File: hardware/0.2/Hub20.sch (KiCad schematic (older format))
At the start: 130 parts, among them J1 USB_C_Receptacle_USB2.0, Q1 DTC123J, Q2 BSS138, SW1 SW_Push, SW10 MX_RGB, SW11 MX_RGB, SW12 MX_RGB, SW13 Rotary_Encoder_Switch, SW14 MX_RGB, SW15 MX_RGB, SW16 MX_RGB, SW17 MX_RGB, SW18 MX_RGB, SW19 MX_RGB, SW2 MX_RGB, SW20 MX_RGB, SW21 MX_RGB, SW22 MX_RGB, SW23 MX_RGB, SW3 MX_RGB, SW4 MX_RGB, SW5 MX_RGB, SW6 MX_RGB, SW7 Rotary_Encoder_Switch, SW8 MX_RGB, SW9 MX_RGB, U1 AP2112K-3.3, U2 USBLC6-2SC6, U3 STM32F072C8Tx

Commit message: layout getting close
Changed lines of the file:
@@
 Wire Wire Line
 	2650 4500 2650 4550
-$Comp
-L power:+3V3 #PWR044
-U 1 1 5EF80615
-P 2750 3950
-F 0 "#PWR044" H 2750 3800 50  0001 C CNN
-F 1 "+3V3" H 2765 4123 50  0000 C CNN
-F 2 "" H 2750 3950 50  0001 C CNN
-F 3 "" H 2750 3950 50  0001 C CNN
-	1    2750 3950
-	1    0    0    -1
-$EndComp
 Wire Wire Line
 	2550 4100 2650 4100
@@
 U 1 1 5F48ECC9
 P 2550 2300
-F 0 "U2" H 2550 2981 50  0000 C CNN
-F 1 "USBLC6-2SC6" H 2550 2890 50  0000 C CNN
+F 0 "U2" H 2375 2600 50  0000 C CNN
+F 1 "USBLC6-2SC6" H 2850 2600 50  0000 C CNN
 F 2 "Package_TO_SOT_SMD:SOT-23-6" H 1800 2700 50  0001 C CNN
 F 3 "http://www2.st.com/resource/en/datasheet/CD00050750.pdf" H 2750 2650 50  0001 C CNN
@@
 $EndComp
 $Comp
-L power:+3V3 #PWR0101
-U 1 1 60B0E43F
-P 1000 6150
-F 0 "#PWR0101" H 1000 6000 50  0001 C CNN
-F 1 "+3V3" H 1015 6323 50  0000 C CNN
-F 2 "" H 1000 6150 50  0001 C CNN
-F 3 "" H 1000 6150 50  0001 C CNN
-	1    1000 6150
-	1    0    0    -1
-$EndComp
-$Comp
-L power:+3V3 #PWR0188
-U 1 1 60B0F88E
-P 8300 2650
-F 0 "#PWR0188" H 8300 2500 50  0001 C CNN
-F 1 "+3V3" H 8315 2823 50  0000 C CNN
-F 2 "" H 8300 2650 50  0001 C CNN
-F 3 "" H 8300 2650 50  0001 C CNN
-	1    8300 2650
-	1    0    0    -1
-$EndComp
-$Comp
-L power:+3V3 #PWR0189
-U 1 1 60B200DB
-P 9800 9800
-F 0 "#PWR0189" H 9800 9650 50  0001 C CNN
-F 1 "+3V3" H 9815 9973 50  0000 C CNN
-F 2 "" H 9800 9800 50  0001 C CNN
-F 3 "" H 9800 9800 50  0001 C CNN
-	1    9800 9800
-	1    0    0    -1
-$EndComp
-$Comp
 L Device:D_Small D26
 U 1 1 5F566ED0
@@
 LED_5V
 NoConn ~ 15850 7300
+$Comp
+L power:+3.3V #PWR0101
+U 1 1 5F3592B8
+P 2750 3950
+F 0 "#PWR0101" H 2750 3800 50  0001 C CNN
+F 1 "+3.3V" H 2765 4123 50  0000 C CNN
+F 2 "" H 2750 3950 50  0001 C CNN
+F 3 "" H 2750 3950 50  0001 C CNN
+	1    2750 3950
+	1    0    0    -1
+$EndComp
+$Comp
+L power:+3.3V #PWR0148
+U 1 1 5F3A0227
+P 1000 6150
+F 0 "#PWR0148" H 1000 6000 50  0001 C CNN
+F 1 "+3.3V" H 1015 6323 50  0000 C CNN
+F 2 "" H 1000 6150 50  0001 C CNN
+F 3 "" H 1000 6150 50  0001 C CNN
+	1    1000 6150
+	1    0    0    -1
+$EndComp
+$Comp
+L power:+3.3V #PWR0149
+U 1 1 5F4789D3
+P 9800 9800
+F 0 "#PWR0149" H 9800 9650 50  0001 C CNN
+F 1 "+3.3V" H 9815 9973 50  0000 C CNN
+F 2 "" H 9800 9800 50  0001 C CNN
+F 3 "" H 9800 9800 50  0001 C CNN
+	1    9800 9800
+	1    0    0    -1
+$EndComp
+$Comp
+L power:+3.3V #PWR0150
+U 1 1 5F4CF7BC
+P 8300 2650
+F 0 "#PWR0150" H 8300 2500 50  0001 C CNN
+F 1 "+3.3V" H 8300 2825 50  0000 C CNN
+F 2 "" H 8300 2650 50  0001 C CNN
+F 3 "" H 8300 2650 50  0001 C CNN
+	1    8300 2650
+	1    0    0    -1
+$EndComp
 $EndSCHEMATC

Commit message: tidy up things
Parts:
- SW1: value SW_Push -> KMR2
- SW13, SW7: value Rotary_Encoder_Switch -> EC11
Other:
- moved on the sheet: C10, C18, C19, C20, C28, C32, C34, C36, C38, C40, C48, C49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

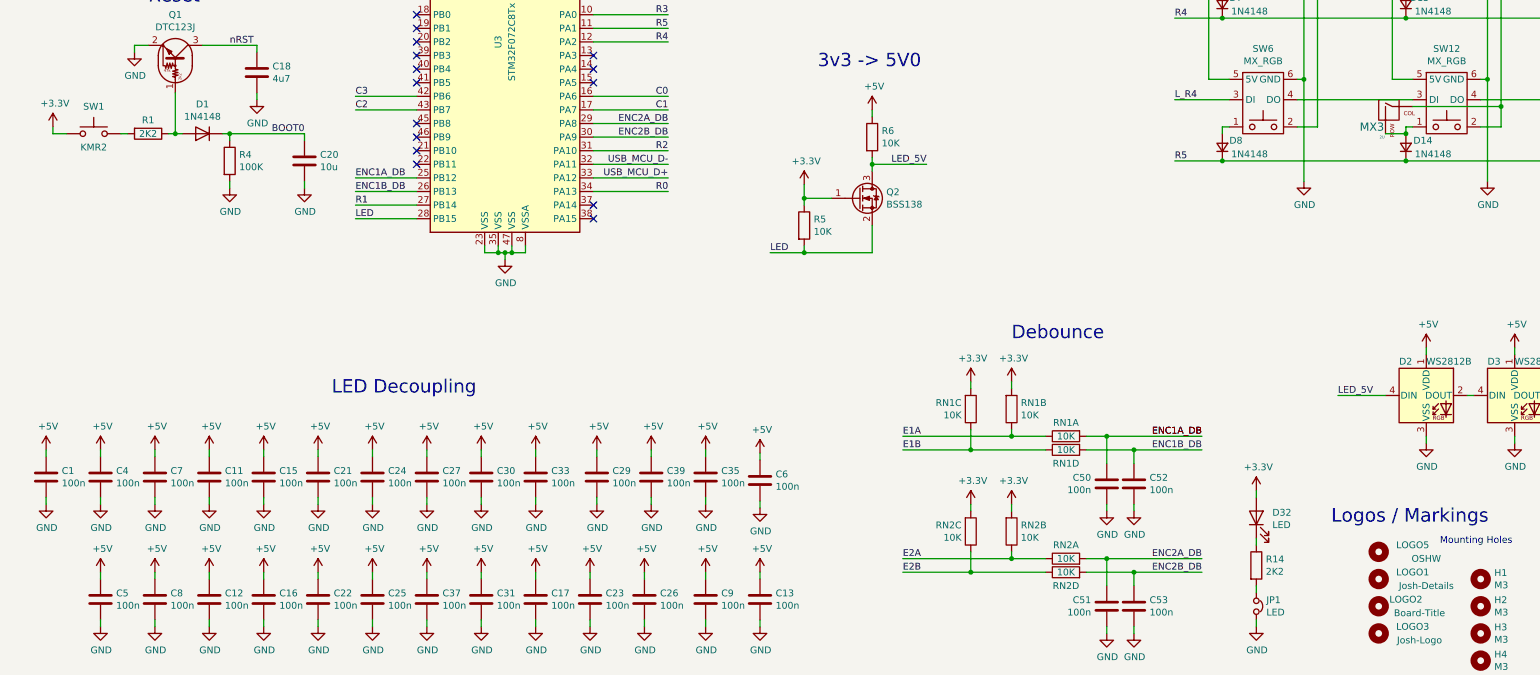
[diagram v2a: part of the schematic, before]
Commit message: side mounted rst + slik cleanup
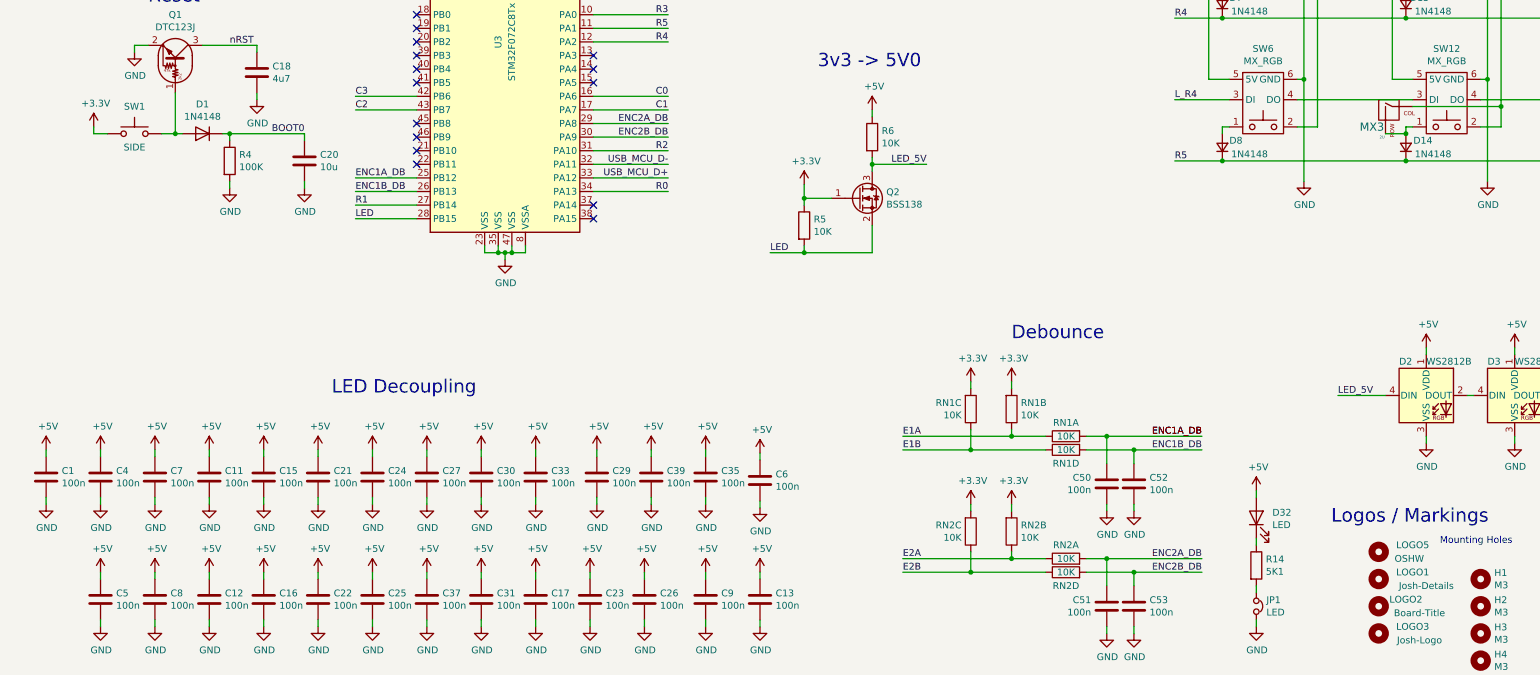
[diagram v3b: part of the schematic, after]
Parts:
- removed R1: 2K2, Resistor_SMD:R_0603_1608Metric, symbol Device:R
- LOGO3: footprint josh-logos:josh-johnson-logo-8_6x1_5 -> josh-logos:josh-johnson-logo-11x2
- LOGO5: footprint josh-logos:OSHW_Logo_3.6x3.6_F.Mask -> josh-logos:OSHW-Logo2_9.8x8mm_Mask
- R14: value 2K2 -> 5K1
- SW1: value KMR2 -> SIDE; footprint josh-buttons-switches:SW_Push_KMR2 -> josh-buttons-switches:Panasonic_EVQPUL_EVQPUC
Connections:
- net +3V3: no longer D32.2 (A)
- net +5V: now also D32.2 (A)
- net at D1.2 (A), Q1.1 (B): now also SW1.2
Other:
- moved on the sheet: SW1
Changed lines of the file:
@@
 F 0 "LOGO3" H 10950 10900 50  0000 C CNN
 F 1 "Josh-Logo" H 11000 10800 50  0000 C CNN
-F 2 "josh-logos:josh-johnson-logo-8_6x1_5" H 10700 10850 50  0001 C CNN
+F 2 "josh-logos:josh-johnson-logo-11x2" H 10700 10850 50  0001 C CNN
 F 3 "~" H 10700 10850 50  0001 C CNN
 	1    10700 10850
@@
 $EndComp
 $Comp
-L Mechanical:MountingHole LOGO2
-U 1 1 5E205A57
-P 10700 10650
-F 0 "LOGO2" H 10900 10700 50  0000 C CNN
-F 1 "Board-Title" H 11000 10600 50  0000 C CNN
-F 2 "josh-logos:board-title" H 10700 10650 50  0001 C CNN
-F 3 "~" H 10700 10650 50  0001 C CNN
-	1    10700 10650
-	1    0    0    -1
-$EndComp
-$Comp
 L Mechanical:MountingHole H3
 U 1 1 5EF4D892
@@
 $EndComp
 $Comp
-L Device:R R1
-U 1 1 5F123A6F
-P 1650 7175
-F 0 "R1" V 1550 7175 50  0000 C CNN
-F 1 "2K2" V 1650 7175 50  0000 C CNN
-F 2 "Resistor_SMD:R_0603_1608Metric" V 1580 7175 50  0001 C CNN
-F 3 "~" H 1650 7175 50  0001 C CNN
-	1    1650 7175
-	0    1    1    0
-$EndComp
-$Comp
 L Switch:SW_Push SW1
 U 1 1 5F124780
-P 1250 7175
-F 0 "SW1" H 1250 7375 50  0000 C CNN
-F 1 "KMR2" H 1250 7075 50  0000 C CNN
-F 2 "josh-buttons-switches:SW_Push_KMR2" H 1250 7375 50  0001 C CNN
-F 3 "~" H 1250 7375 50  0001 C CNN
-	1    1250 7175
+P 1550 7175
+F 0 "SW1" H 1550 7375 50  0000 C CNN
+F 1 "SIDE" H 1550 7075 50  0000 C CNN
+F 2 "josh-buttons-switches:Panasonic_EVQPUL_EVQPUC" H 1550 7375 50  0001 C CNN
+F 3 "~" H 1550 7375 50  0001 C CNN
+	1    1550 7175
 	1    0    0    -1
 $EndComp
@@
 $EndComp
 Wire Wire Line
-	950  7125 950  7175
+	1250 7125 1250 7175
 Wire Wire Line
-	950  7175 1050 7175
-Wire Wire Line
-	1450 7175 1500 7175
-Wire Wire Line
-	1800 7175 1850 7175
+	1250 7175 1350 7175
 Wire Wire Line
 	1850 6875 1850 7175
@@
 P 9800 10350
 F 0 "R14" H 9870 10396 50  0000 L CNN
-F 1 "2K2" H 9870 10305 50  0000 L CNN
+F 1 "5K1" H 9870 10305 50  0000 L CNN
 F 2 "Resistor_SMD:R_0603_1608Metric" V 9730 10350 50  0001 C CNN
 F 3 "~" H 9800 10350 50  0001 C CNN
@@
 P 10700 10250
 F 0 "LOGO5" H 10950 10300 50  0000 C CNN
-F 1 "OSHW" H 11050 10200 50  0000 C CNN
-F 2 "josh-logos:OSHW_Logo_3.6x3.6_F.Mask" H 10700 10250 50  0001 C CNN
+F 1 "OSHW" H 10925 10200 50  0000 C CNN
+F 2 "josh-logos:OSHW-Logo2_9.8x8mm_Mask" H 10700 10250 50  0001 C CNN
 F 3 "~" H 10700 10250 50  0001 C CNN
 	1    10700 10250
@@
 L power:+3.3V #PWR0148
 U 1 1 5F3A0227
-P 950 7125
-F 0 "#PWR0148" H 950 6975 50  0001 C CNN
-F 1 "+3.3V" H 965 7298 50  0000 C CNN
-F 2 "" H 950 7125 50  0001 C CNN
-F 3 "" H 950 7125 50  0001 C CNN
-	1    950  7125
-	1    0    0    -1
-$EndComp
-$Comp
-L power:+3.3V #PWR0149
-U 1 1 5F4789D3
-P 9800 9800
-F 0 "#PWR0149" H 9800 9650 50  0001 C CNN
-F 1 "+3.3V" H 9815 9973 50  0000 C CNN
-F 2 "" H 9800 9800 50  0001 C CNN
-F 3 "" H 9800 9800 50  0001 C CNN
-	1    9800 9800
+P 1250 7125
+F 0 "#PWR0148" H 1250 6975 50  0001 C CNN
+F 1 "+3.3V" H 1265 7298 50  0000 C CNN
+F 2 "" H 1250 7125 50  0001 C CNN
+F 3 "" H 1250 7125 50  0001 C CNN
+	1    1250 7125
 	1    0    0    -1
 $EndComp
@@
 3v3 -> 5V0
 Connection ~ 5275 4600
+$Comp
+L Mechanical:MountingHole LOGO2
+U 1 1 5E205A57
+P 10700 10650
+F 0 "LOGO2" H 10900 10700 50  0000 C CNN
+F 1 "Board-Title" H 11000 10600 50  0000 C CNN
+F 2 "josh-logos:board-title" H 10700 10650 50  0001 C CNN
+F 3 "~" H 10700 10650 50  0001 C CNN
+	1    10700 10650
+	1    0    0    -1
+$EndComp
+$Comp
+L power:+5V #PWR0149
+U 1 1 5F4C0452
+P 9800 9800
+F 0 "#PWR0149" H 9800 9650 50  0001 C CNN
+F 1 "+5V" H 9815 9973 50  0000 C CNN
+F 2 "" H 9800 9800 50  0001 C CNN
+F 3 "" H 9800 9800 50  0001 C CNN
+	1    9800 9800
+	1    0    0    -1
+$EndComp
+Wire Wire Line
+	1750 7175 1850 7175
 $EndSCHEMATC

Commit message: update BOM
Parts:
- added D31, D33, D34, D35, D36, D37, D38, D39, D40, D41, D42, D43, D44, D45, D46, D47, D48, D49, D50, D51: SK6812MINI-E, josh-keyboard:DUMMY_SK6812MINI-E, symbol Mechanical:MountingHole
- C1, C11, C12, C13, C15, C16, C17, C21, C22, C23, C24, C25, C26, C27, C29, C30, C31, C33, C35, C36, C37, C38, C39, C4, C40, C48, C49, C5, C50, C51, C52, C53, C6, C7, C8, C9: DigiKey (none) -> 1276-1000-1-ND; LCSC (none) -> C1591; MPN (none) -> CL10B104KB8NNNC; Manufacturer (none) -> Samsung Electro-Mechanics; Substitue Allowed? (none) -> Y - X5R or better
- C10, C19, C28, C32, C34: DigiKey (none) -> 1276-1866-1-ND; LCSC (none) -> C29936; MPN (none) -> CL10A105MP8NNNC; Manufacturer (none) -> Samsung Electro-Mechanics; Substitue Allowed? (none) -> Y - X5R or better
- C14, C20: DigiKey (none) -> 1276-1871-1-ND; LCSC (none) -> C85713; MPN (none) -> CL10A106MP8NNNC; Manufacturer (none) -> Samsung Electro-Mechanics; Substitue Allowed? (none) -> Y - X5R or better
- C18: DigiKey (none) -> 1276-1905-1-ND; LCSC (none) -> C307473; MPN (none) -> CL10A475MP8NNNC; Manufacturer (none) -> Samsung Electro-Mechanics; Substitue Allowed? (none) -> Y - X5R or better
- D1, D10, D11, D12, D13, D14, D16, D18, D19, D20, D21, D22, D24, D25, D26, D27, D28, D29, D4, D5, D6, D7, D8: DigiKey (none) -> 1N4148W-FDICT-ND; LCSC (none) -> C83528; MPN (none) -> 1N4148W-7-F; Manufacturer (none) -> Diodes Inc; Substitue Allowed? (none) -> Y - Any 1N4148
- D15, D17, D2, D23, D3, D30, D9: DigiKey (none) -> 1528-1104-ND; LCSC (none) -> C114586; MPN (none) -> WS2812B; Manufacturer (none) -> Worldsemi; Notes (none) -> Black prefered, but white also suitable; Substitue Allowed? (none) -> N
- D32: LCSC (none) -> C268294; MPN (none) -> OSK40603C1E; Manufacturer (none) -> OptoSupply; Substitue Allowed? (none) -> Y - Any Pink / Purple
- F1: DigiKey (none) -> 507-1813-1-ND; LCSC (none) -> C66452; MPN (none) -> 0ZCK0050FF2E; Manufacturer (none) -> Bel Fuse; Notes (none) -> LCSC: Substitute PN; Substitue Allowed? (none) -> Y - 500mA hold / 1A trip
- FB1: DigiKey (none) -> 490-5258-1-ND; LCSC (none) -> C85833; MPN (none) -> BLM18KG601SN1D; Manufacturer (none) -> Murata; Substitue Allowed? (none) -> Y - 600R, > 1A current
- H1, H2, H3, H4, JP1, LOGO1, LOGO2, LOGO3, LOGO5, MX1, MX2, MX3, MX4, MX5, MX6, SW10, SW11, SW12, SW14, SW15, SW16, SW17, SW18, SW19, SW2, SW20, SW21, SW22, SW23, SW3, SW4, SW5, SW6, SW8, SW9: DNP (none) -> DNP
- J1: LCSC (none) -> C319148; MPN (none) -> U262-161N-4BVC11; Manufacturer (none) -> XKB Enterprise; Notes (none) -> Cannot source from DigiKey; Substitue Allowed? (none) -> Y - Footprint / pinout compatiable
- Q1: DigiKey (none) -> DTC123JKAT146CT-ND; LCSC (none) -> C111724; MPN (none) -> DTC123JKAT146; Manufacturer (none) -> ROHM Semicon; Substitue Allowed? (none) -> Y - Any DTC123J
- Q2: DigiKey (none) -> BSS138CT-ND; LCSC (none) -> C52895; MPN (none) -> BSS138; Manufacturer (none) -> ON Semiconductor; Substitue Allowed? (none) -> Y - Any BSS138
- R14, R2, R3: DigiKey (none) -> 118-CR0603-JW-512ELFCT-ND; LCSC (none) -> C14677; MPN (none) -> CR0603-JW-512ELF; Manufacturer (none) -> Bourns; Notes (none) -> LCSC: Substitute PN; Substitue Allowed? (none) -> Y - Same spec
- R4: DigiKey (none) -> CR0603-JW-104ELFCT-ND; LCSC (none) -> C100048; MPN (none) -> CR0603-JW-104ELF; Manufacturer (none) -> Bourns; Notes (none) -> LCSC: Substitute PN; Substitue Allowed? (none) -> Y - Same spec
- R5, R6: DigiKey (none) -> CR0603-JW-103ELFCT-ND; LCSC (none) -> C144116; MPN (none) -> CR0603-JW-103ELF; Manufacturer (none) -> Bourns; Notes (none) -> LCSC: Substitute PN; Substitue Allowed? (none) -> Y - Same spec
- RN1, RN2: DigiKey (none) -> RAVF164DJT10K0CT-ND; LCSC (none) -> C107374; MPN (none) -> RAVF164DJT10K0; Manufacturer (none) -> Bourns; Notes (none) -> LCSC: Substitute PN; Substitue Allowed? (none) -> Y - Same spec
- SW1: value SIDE -> EVQPUL; DigiKey (none) -> P10853SCT-ND; LCSC (none) -> C397351; MPN (none) -> EVQ-PUL02K; Manufacturer (none) -> Panasonic; Notes (none) -> LCSC: Substitute PN; Substitue Allowed? (none) -> Y - Same footprint
- SW13, SW7: DNP (none) -> DNP; DigiKey (none) -> PEC11L-4120F-S0020-ND; MPN (none) -> PEC11L-4120F-S0020; Manufacturer (none) -> Bourns; Notes (none) -> Similar to: https://www.aliexpress.com/item/32839106848.html; Substitue Allowed? (none) -> Y - 20 pulse per revolution
- U1: DigiKey (none) -> AP2112K-3.3TRG1DICT-ND; LCSC (none) -> C51118; MPN (none) -> AP2112K-3.3TRG1; Manufacturer (none) -> Diodes Incorporated; Substitue Allowed? (none) -> N
- U2: DigiKey (none) -> 497-5235-1-ND; LCSC (none) -> C7519; MPN (none) -> USBLC6-2SC6; Manufacturer (none) -> STMicroelectronics; Substitue Allowed? (none) -> N
- U3: DigiKey (none) -> 497-17359-1-ND; LCSC (none) -> C80488; MPN (none) -> STM32F072C8T6; Manufacturer (none) -> STMicroelectronics; Substitue Allowed? (none) -> N
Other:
- note added: "SK6812 Mini E's are part of the key \nswitch footprint, so add placeholders \nfor the LEDs themselves.\n\nThese will generate the correct \nXY positions for the LEDs when\nplaced upon the MX footprint.\n\nIt also ensures they show up as a\nline item on the BOM."
- moved on the sheet: D10, D11, D12, D13, D14, D16, D18, D19, D20, D21, D22, D24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

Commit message: limit 2U to 3 pin only
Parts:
- MX1, MX2: footprint josh-keyboard:MXOnly-2U-NoLED -> josh-keyboard:MXOnly-2U-NoLED-3PIN
- MX3, MX4, MX5, MX6: footprint josh-keyboard:MXOnly-2U-ReversedStabilizers-NoLED -> josh-keyboard:MXOnly-2U-ReversedStabilizers-NoLED-3PIN
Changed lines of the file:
@@
 F 0 "MX4" H 11250 6875 60  0000 C CNN
 F 1 "2U" H 11325 6800 20  0000 C CNN
-F 2 "josh-keyboard:MXOnly-2U-ReversedStabilizers-NoLED" H 10775 6950 60  0001 C CNN
+F 2 "josh-keyboard:MXOnly-2U-ReversedStabilizers-NoLED-3PIN" H 10775 6950 60  0001 C CNN
 F 3 "" H 10775 6950 60  0001 C CNN
 F 4 "DNP" H 11400 6975 50  0001 C CNN "DNP"
@@
 F 0 "MX3" H 9900 6875 60  0000 C CNN
 F 1 "2U" H 9975 6800 20  0000 C CNN
-F 2 "josh-keyboard:MXOnly-2U-ReversedStabilizers-NoLED" H 9425 6950 60  0001 C CNN
+F 2 "josh-keyboard:MXOnly-2U-ReversedStabilizers-NoLED-3PIN" H 9425 6950 60  0001 C CNN
 F 3 "" H 9425 6950 60  0001 C CNN
 F 4 "DNP" H 10050 6975 50  0001 C CNN "DNP"
@@
 F 0 "MX6" H 12700 5825 60  0000 C CNN
 F 1 "2U" H 12750 5750 20  0000 C CNN
-F 2 "josh-keyboard:MXOnly-2U-ReversedStabilizers-NoLED" H 12225 5900 60  0001 C CNN
+F 2 "josh-keyboard:MXOnly-2U-ReversedStabilizers-NoLED-3PIN" H 12225 5900 60  0001 C CNN
 F 3 "" H 12225 5900 60  0001 C CNN
 F 4 "DNP" H 12850 5925 50  0001 C CNN "DNP"
@@
 F 0 "MX5" H 12700 3675 60  0000 C CNN
 F 1 "2U" H 12775 3600 20  0000 C CNN
-F 2 "josh-keyboard:MXOnly-2U-ReversedStabilizers-NoLED" H 12225 3750 60  0001 C CNN
+F 2 "josh-keyboard:MXOnly-2U-ReversedStabilizers-NoLED-3PIN" H 12225 3750 60  0001 C CNN
 F 3 "" H 12225 3750 60  0001 C CNN
 F 4 "DNP" H 12850 3775 50  0001 C CNN "DNP"
@@
 F 0 "MX2" H 8500 5950 60  0000 C CNN
 F 1 "2U" H 8550 5875 20  0000 C CNN
-F 2 "josh-keyboard:MXOnly-2U-NoLED" H 8075 5900 60  0001 C CNN
+F 2 "josh-keyboard:MXOnly-2U-NoLED-3PIN" H 8075 5900 60  0001 C CNN
 F 3 "" H 8075 5900 60  0001 C CNN
 F 4 "DNP" H 8700 5925 50  0001 C CNN "DNP"
@@
 F 0 "MX1" H 8550 3675 60  0000 C CNN
 F 1 "2U" H 8625 3600 20  0000 C CNN
-F 2 "josh-keyboard:MXOnly-2U-NoLED" H 8075 3750 60  0001 C CNN
+F 2 "josh-keyboard:MXOnly-2U-NoLED-3PIN" H 8075 3750 60  0001 C CNN
 F 3 "" H 8075 3750 60  0001 C CNN
 F 4 "DNP" H 8700 3775 50  0001 C CNN "DNP"

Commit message: update fuse values
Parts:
- F1: value 500mA -> 1A; DigiKey 507-1813-1-ND -> F2774CT-ND; LCSC C66452 -> C80270; MPN 0ZCK0050FF2E -> 0805L100WR; Manufacturer Bel Fuse -> Littelfuse; Notes LCSC: Substitute PN -> (none)
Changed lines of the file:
@@
 P 2850 1500
 F 0 "F1" V 2625 1500 50  0000 C CNN
-F 1 "500mA" V 2716 1500 50  0000 C CNN
+F 1 "1A" V 2716 1500 50  0000 C CNN
 F 2 "josh-passives-smt:Fuse_0805_2012Metric" H 2900 1300 50  0001 L CNN
 F 3 "~" H 2850 1500 50  0001 C CNN
-F 4 "507-1813-1-ND" H 2850 1500 50  0001 C CNN "DigiKey"
-F 5 "C66452" H 2850 1500 50  0001 C CNN "LCSC"
-F 6 "0ZCK0050FF2E" H 2850 1500 50  0001 C CNN "MPN"
-F 7 "Bel Fuse" H 2850 1500 50  0001 C CNN "Manufacturer"
-F 8 "LCSC: Substitute PN" H 2850 1500 50  0001 C CNN "Notes"
+F 4 "F2774CT-ND" H 2850 1500 50  0001 C CNN "DigiKey"
+F 5 "C80270" H 2850 1500 50  0001 C CNN "LCSC"
+F 6 "0805L100WR" H 2850 1500 50  0001 C CNN "MPN"
+F 7 "Littelfuse" H 2850 1500 50  0001 C CNN "Manufacturer"
+F 8 "" H 2850 1500 50  0001 C CNN "Notes"
 F 9 "Y - 500mA hold / 1A trip" H 2850 1500 50  0001 C CNN "Substitue Allowed?"
 	1    2850 1500
